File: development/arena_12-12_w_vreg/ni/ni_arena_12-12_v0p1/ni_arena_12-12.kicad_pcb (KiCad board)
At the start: 4 copper layers, 228.6 x 228.6 mm, 126 parts, among them J1 Barrel_Jack, J2 NI_TE_68pos, P1 CONN15, P10 CONN15, P11 CONN15, P12 CONN15, P2 CONN15, P3 CONN15, P4 CONN15, P5 CONN15, P6 CONN15, P7 CONN15, P8 CONN15, P9 CONN15, Q2 MOSFET_NCHAN, SW1 SW_SPDT, U1 TXB0108PW, U10 TPS564201DDC, U11 TPS564201DDC, U12 TPS564201DDC, U13 TPS564201DDC, U14 TPS564201DDC, U15 TPS564201DDC, U16 TPS564201DDC, U17 TPS564201DDC, U18 AP2112K-3.3, U2 TXB0108PW, U3 TXB0108PW, U4 TXB0108PW, U5 TXB0108PW, U6 TPS564201DDC, U7 TPS564201DDC, U8 TPS564201DDC, U9 TPS564201DDC

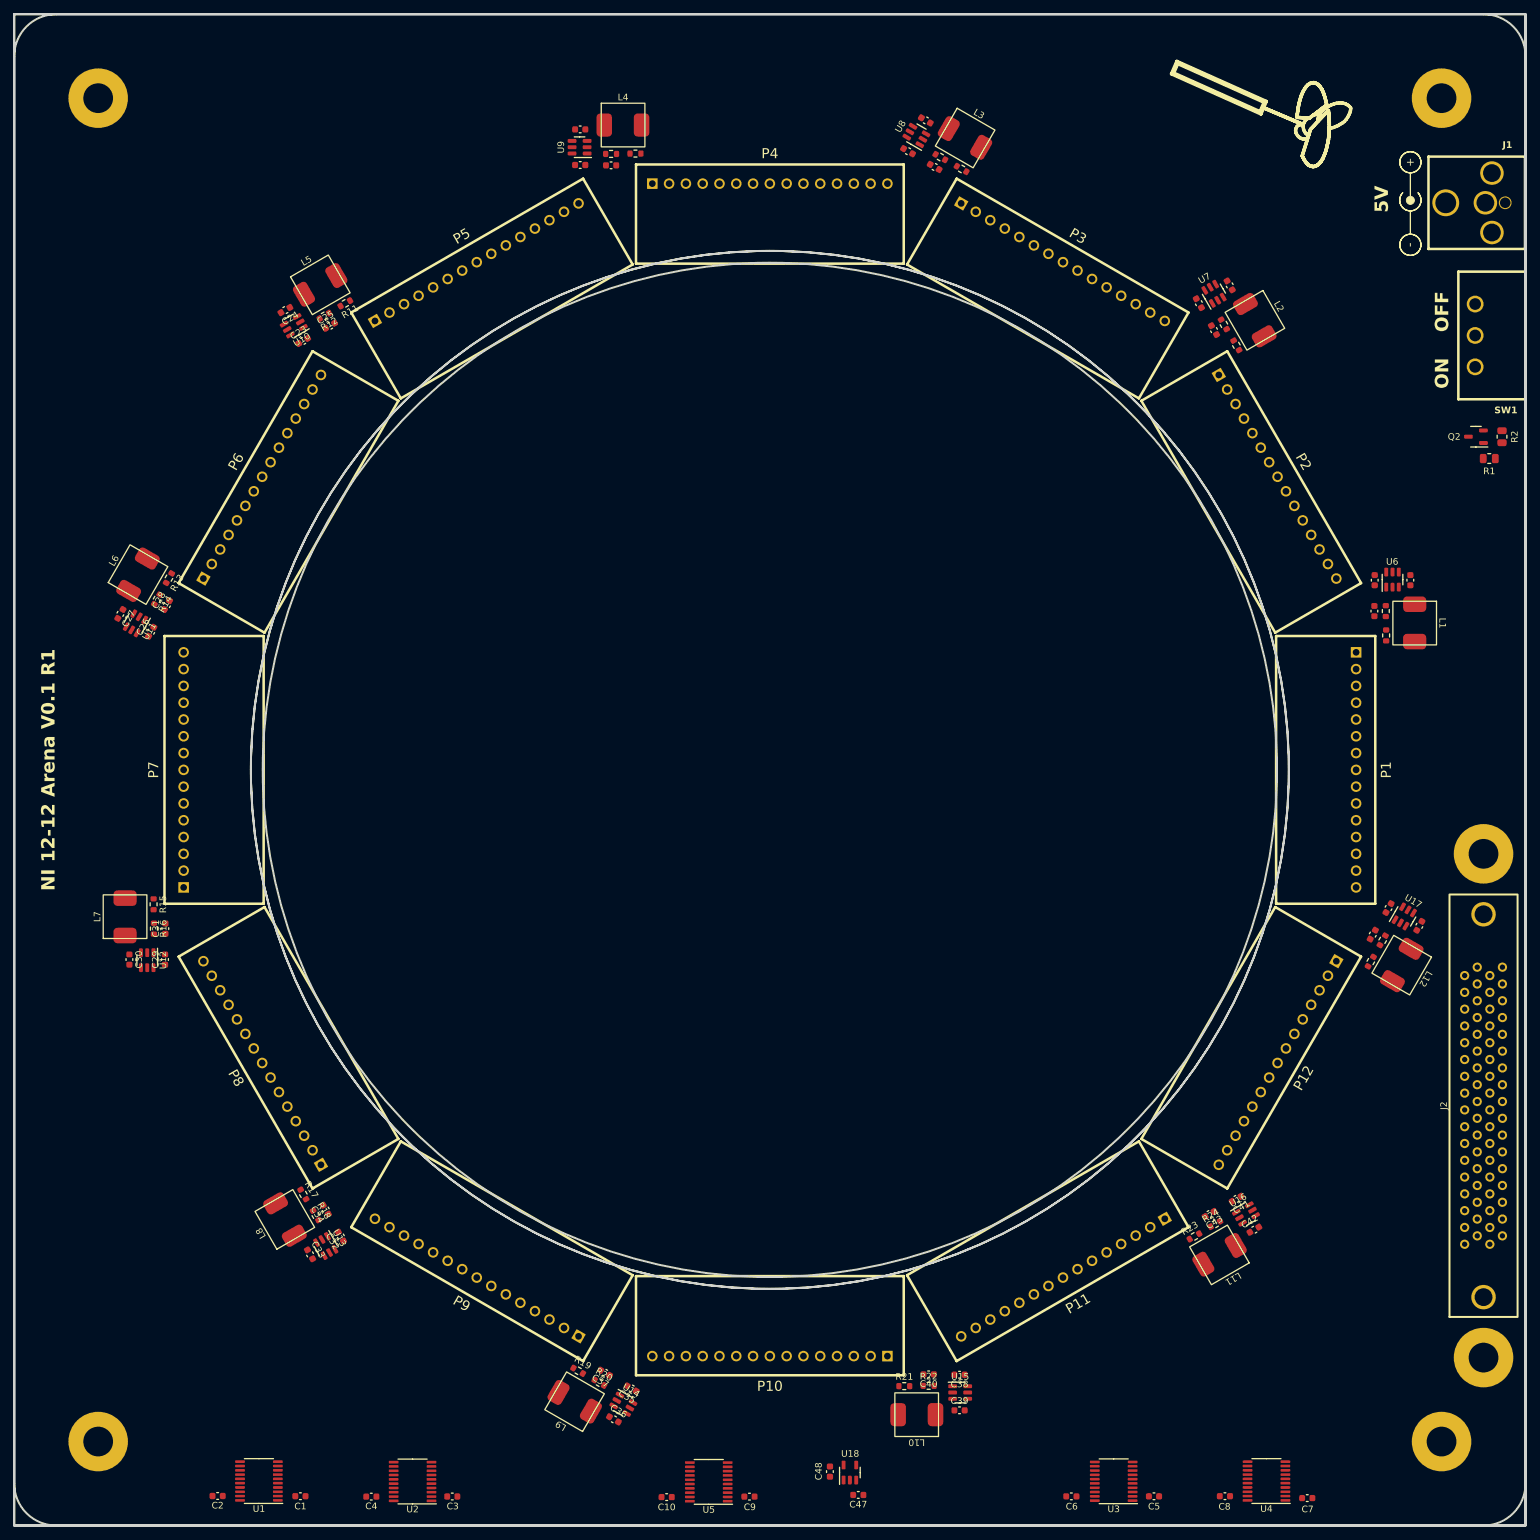
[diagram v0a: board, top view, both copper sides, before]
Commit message: Added 3D model of inductor for vreg designs.
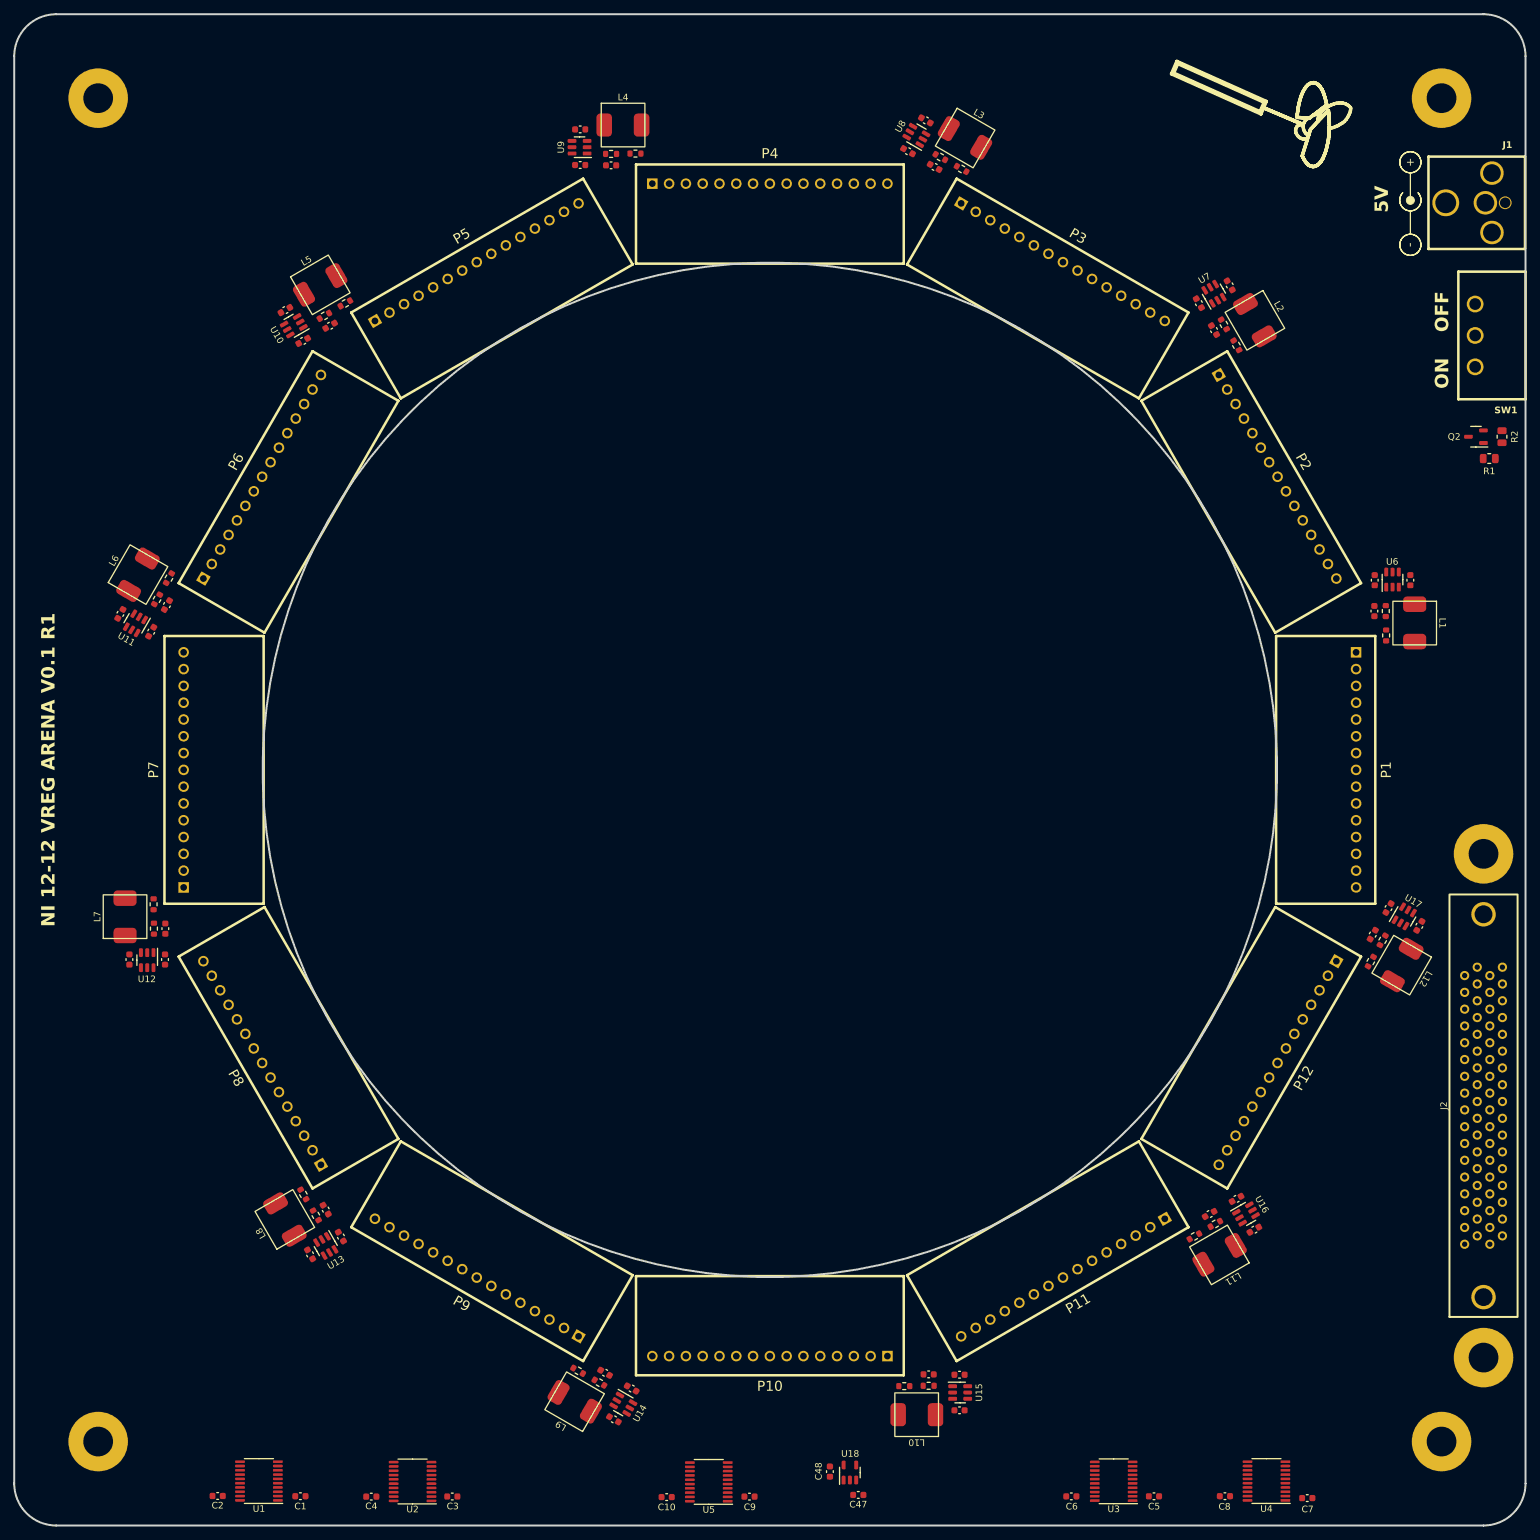
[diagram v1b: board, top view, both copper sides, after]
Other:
- outline, holes or cut-outs redrawn
- board text added: "NI 12-12 VREG ARENA V0.1 R1"
- board text removed: "NI 12-12 Arena V0.1 R1"

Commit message: Worked on routing for ni and teensy vreg arenas.
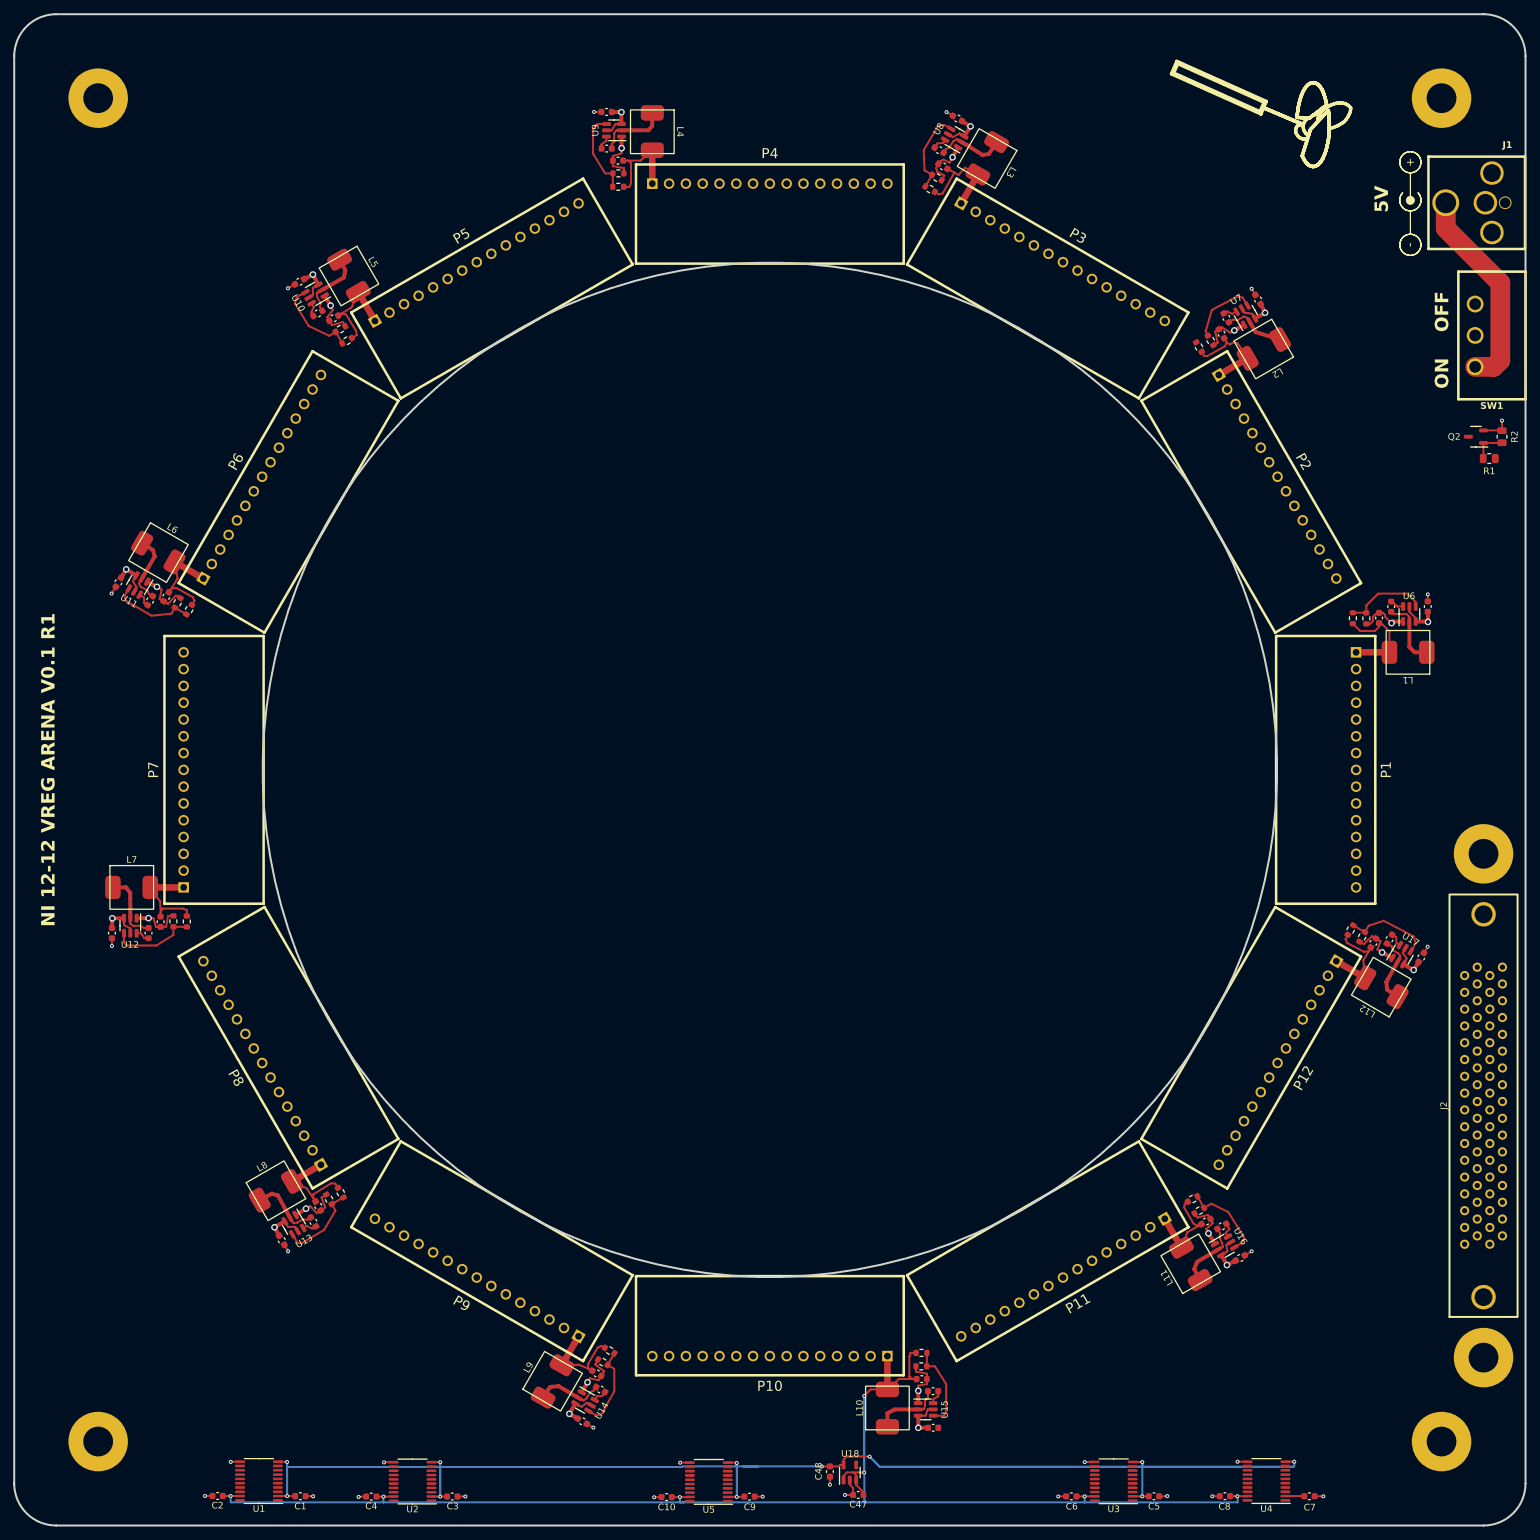
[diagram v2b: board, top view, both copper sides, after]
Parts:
- C11: value 100nF -> 10uF
- C12: value 10uF -> 100nF
- moved C14 8.96 mm to (251.6, 106.6), turned to 120 degrees
- moved C23 8.96 mm to (106.6, 104.0), turned to -150 degrees
- moved C32 8.96 mm to (104.0, 249.0), turned to -60 degrees
- moved C41 8.96 mm to (249.0, 251.6), turned to 30 degrees
- moved C38 8.96 mm to (202.5, 277.3), turned to 0 degrees
- moved C17 8.96 mm to (206.2, 79.3), turned to 150 degrees
- moved C26 8.96 mm to (79.3, 149.4), turned to -120 degrees
- moved C35 8.96 mm to (149.4, 276.3), turned to -30 degrees
- moved C44 8.96 mm to (276.3, 206.2), turned to 60 degrees
- moved C11 8.96 mm to (277.3, 153.1), turned to 90 degrees
- moved C20 8.96 mm to (153.1, 78.3), turned to 180 degrees
- moved C29 8.96 mm to (78.3, 202.5), turned to -90 degrees
- moved U15 5.80 mm to (201.4, 274.5)
- moved U6 5.80 mm to (274.5, 154.2)
- moved U12 5.80 mm to (81.1, 201.4)
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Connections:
- net Net-(SW1-A) renamed /Power & Voltage Regulators/SW_VCC
- C11 pad 1: Net-(U6-VBST) -> VCC
- C11 pad 2: Net-(U6-SW) -> GND
- C12 pad 1: VCC -> Net-(U6-VBST)
- C12 pad 2: GND -> Net-(U6-SW)
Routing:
- net /Level Shifters/POW.5V_HDR_10: track 0.00 -> 213.9 mm, vias 0 -> 7
- net +3.3V: track 0.00 -> 198.4 mm, vias 0 -> 11
- net GND: track 0.00 -> 136.0 mm, vias 0 -> 41
- net VCC: track 0.00 -> 73.6 mm, vias 0 -> 12
- net /Power & Voltage Regulators/SW_VCC: track 0.00 -> 31.5 mm
- net /Level Shifters/POW.5V_HDR_5: track 0.00 -> 15.7 mm
- net /Level Shifters/POW.5V_HDR_3: track 0.00 -> 15.6 mm
- net /Level Shifters/POW.5V_HDR_1: track 0.00 -> 15.5 mm
- net /Level Shifters/POW.5V_HDR_2: track 0.00 -> 15.3 mm
- net /Level Shifters/POW.5V_HDR_4: track 0.00 -> 15.2 mm
- net /Level Shifters/POW.5V_HDR_7: track 0.00 -> 15.2 mm
- net /Level Shifters/POW.5V_HDR_6: track 0.00 -> 15.1 mm
- net /Level Shifters/POW.5V_HDR_8: track 0.00 -> 15.1 mm
- net /Level Shifters/POW.5V_HDR_12: track 0.00 -> 15.0 mm
- net /Level Shifters/POW.5V_HDR_11: track 0.00 -> 14.9 mm
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- added copper zone on In1.Cu, net GND
- added copper zone on In2.Cu, net VCC
